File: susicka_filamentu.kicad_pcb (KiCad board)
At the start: 4 copper layers, 70 x 100 mm, 108 parts, among them J10 NTC 100k B3950, J11 SHT40 #2, J12 GPIO rezerva, J13 Tepelna pojistka, J2 Conn_01x03, J3 Conn_01x04, J4 PJ-102AH, J5 Topeni 24V, J6 SHT4x, J7 HX711, J8 Ventilator 24V, J9 Odtah 24V, Q1 SiS434DN, Q2 AO3422, Q3 AOD4185, Q4 AO3422, SW1 Tlacitko, U1 RP2350A-QFN60, U2 RM2, U3 W25Q128JVS, U4 AP63203WU, Y1 ABM8-272-T3 12MHz

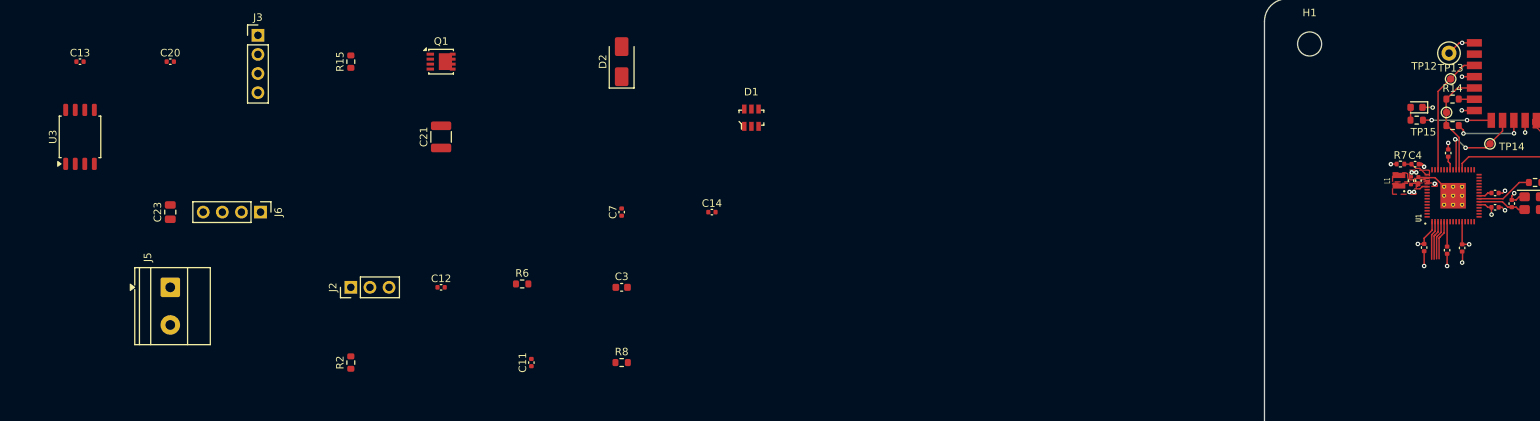
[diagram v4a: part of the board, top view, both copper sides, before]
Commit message: Place and route RP2350 decoupling capacitors
- C11 (pin 30), C13 (pins 44+45), C14 (pins 53+54) next to their pins
- C12 for pin 38 via +3V3 plane: pin 38 has a via under the package,
  C12 above C13 with its own +3V3 via and shared GND via
- C9/C16/C17/C8/C10/C15 kept; zones refilled (fixes GND via vs +1V1 zone clearance)

Co-Authored-By: Claude Opus 5.5 <noreply@anthropic.com>
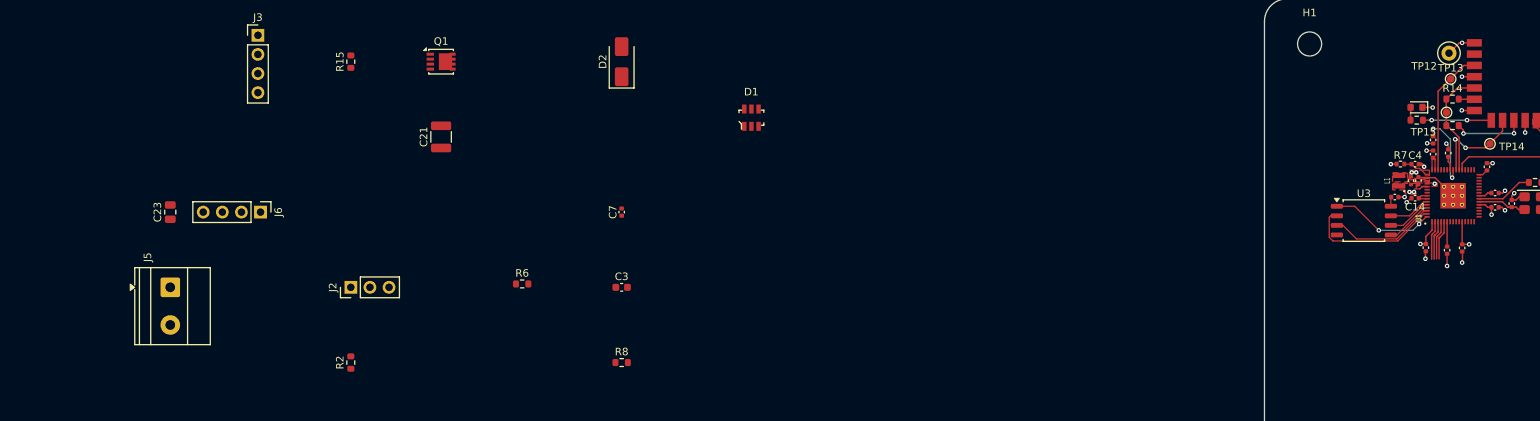
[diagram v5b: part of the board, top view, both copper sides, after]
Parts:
- moved C13 180.3 mm to (209.5, 58.5), turned to 90 degrees
- moved U3 171.0 mm to (200.3, 67.4), turned to 0 degrees
- moved C20 163.8 mm to (204.4, 64.2)
- moved C12 133.3 mm to (209.5, 56.6), turned to -90 degrees
- moved C11 129.7 mm to (216.7, 60.2)
- moved C14 93.5 mm to (207.1, 64.4), turned to 180 degrees
- moved C10 0.23 mm to (208.6, 71.0)
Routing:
- net /flash/QSPI_SD1: track 0.00 -> 19.4 mm
- net +3V3: track 18.1 -> 36.4 mm, vias 7 -> 9
- net /flash/QSPI_SD2: track 0.00 -> 14.4 mm
- net /flash/QSPI_SS: track 0.00 -> 14.1 mm, vias 0 -> 2
- net /flash/QSPI_SD0: track 0.00 -> 6.43 mm
- net /flash/QSPI_SCLK: track 0.00 -> 5.96 mm
- net /flash/QSPI_SD3: track 0.00 -> 5.60 mm
- net GND: track 37.1 -> 41.8 mm, vias 20 -> 25

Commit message: Update PCB layout (current working version)
Co-Authored-By: Claude Haiku 5.5 <noreply@anthropic.com>
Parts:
- moved C25 224.7 mm to (238.2, 91.0)
- moved D4 222.2 mm to (236.7, 104.9)
- moved R19 219.3 mm to (242.2, 105.2)
- moved F1 208.5 mm to (237.0, 121.5), turned to 90 degrees
- moved Q3 204.1 mm to (237.1, 112.6), turned to -90 degrees
- moved D5 198.1 mm to (237.2, 99.5), turned to 180 degrees
- moved L2 134.6 mm to (166.3, 99.9), turned to 90 degrees
- moved C22 126.9 mm to (163.0, 100.7), turned to 90 degrees
- moved C23 121.3 mm to (160.4, 90.8)
- moved U4 114.3 mm to (159.7, 101.1)
- moved C21 91.1 mm to (155.8, 103.1), turned to -90 degrees
- moved C24 82.3 mm to (164.8, 90.7)
- moved J4 27.6 mm to (241.2, 131.5)
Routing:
- net +1V1: track 8.51 -> 36.5 mm, vias 2 -> 5
- net +3V3: track 36.4 -> 48.9 mm, vias 9 -> 13
- net Net-(U4-SW): track 0.00 -> 5.77 mm
- net GND: track 41.8 -> 45.8 mm, vias 25 -> 35
- net Net-(U4-BST): track 0.00 -> 2.24 mm
- added copper zone on In2.Cu, net +3V3
- added copper zone on F.Cu, net 24V
- added copper zone on F.Cu, net 24V_IN
- added copper zone on In1.Cu, net GND
- added copper zone on In2.Cu, net GND
- added copper zone on F.Cu, net Net-(D4-A)
- added copper zone on F.Cu, net Net-(Q3-D)

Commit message: Layout: I2C pull-ups, test point properties, power section progress
- R21/R22 (I2C1) and R26/R27 (I2C0) placed and routed
- test point fabrication property on placed TPs
- J6 SDA/SCL order swapped in schematic for routing
- J1 (USB, DNP) excluded from board

Co-Authored-By: Claude Opus 5.5 <noreply@anthropic.com>
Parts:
- removed C3: 4,7n, Capacitor_SMD:C_0603_1608Metric
- removed D1: USBLC6-2SC6, digikey-footprints:SOT23-6L
- removed R2, R3: 5,1k, Resistor_SMD:R_0603_1608Metric
- removed R4, R5: 27, Resistor_SMD:R_0603_1608Metric
- removed R6: 1M, Resistor_SMD:R_0603_1608Metric
- moved J11 231.3 mm to (233.1, 80.5), turned to 180 degrees
- moved SW1 220.1 mm to (243.6, 69.8)
- moved C27 217.3 mm to (235.6, 79.3), turned to 90 degrees
- moved R27 210.1 mm to (225.4, 71.1), turned to -90 degrees
- moved R26 206.1 mm to (223.5, 73.5), turned to 90 degrees
- moved R22 194.5 mm to (210.4, 81.2), turned to 90 degrees
- moved R21 191.1 mm to (207.9, 81.2), turned to 90 degrees
- moved TP9 191.0 mm to (229.9, 72.0)
- moved TP8 188.4 mm to (229.7, 74.5)
- moved TP1 183.3 mm to (232.4, 91.7)
- moved TP10 179.6 mm to (217.0, 74.7)
- moved J3 179.1 mm to (231.5, 60.4)
- moved TP11 174.0 mm to (219.7, 74.5)
- moved TP2 170.0 mm to (213.8, 86.6)
- moved TP7 169.9 mm to (210.6, 74.2), turned to 90 degrees
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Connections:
- J6 pad 3: SDA -> SCL
- J6 pad 4: SCL -> SDA
- J7 pad 3: HX711_DT -> HX711_SCK
- J7 pad 4: HX711_SCK -> HX711_DT
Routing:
- net BTN: track 0.00 -> 31.6 mm, vias 0 -> 2
- net +3V3: track 48.9 -> 79.8 mm, vias 13 -> 28
- net SDA0: track 0.00 -> 22.9 mm
- net SCL0: track 0.00 -> 21.4 mm
- net Net-(J3-Pin_4): track 0.00 -> 20.9 mm, vias 0 -> 2
- net SWCLK: track 0.00 -> 17.5 mm
- net SWDIO: track 0.00 -> 17.1 mm
- net HX711_SCK: track 0.00 -> 16.0 mm
- net HX711_DT: track 0.00 -> 13.9 mm
- net GND: track 45.8 -> 59.6 mm, vias 35 -> 78
- net SDA: track 5.20 -> 13.9 mm
- net SCL: track 5.23 -> 13.4 mm
- net Net-(J2-Pin_2): track 0.00 -> 3.20 mm
- net Net-(U1-GPIO1): track 5.22 -> 8.15 mm
- net Net-(J2-Pin_1): track 0.00 -> 2.82 mm
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- removed copper zone on In2.Cu, net GND

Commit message: Layout review fixes and JLCPCB fabrication outputs
- In2: GND pour over the whole board (priority 0) below the 3V3 zones
- Silkscreen: +/- marks of J5, J8, J9 moved out from under the terminal
  blocks; D4 and TP13 labels moved to visible spots
- TP12 moved away from the RM2 antenna keep-out, J4 shifted up,
  R20 220R so the D6 LED is visible at 3.3 V
- NTC (J10, R25, C26, TP19) excluded from this prototype board
- gerber/: fresh Gerber + Excellon export, JLCPCB zip, ordering notes
- CLAUDE.md, .claude/pamet.md: review results and decisions

Co-Authored-By: Claude Opus 5.5 <noreply@anthropic.com>
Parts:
- removed C26: 100nF, Capacitor_SMD:C_0402_1005Metric
- removed J10: NTC 100k B3950, Connector_PinHeader_2.54mm:PinHeader_1x02_P2.54mm_Vertical
- removed R25: 22k, Resistor_SMD:R_0603_1608Metric
- removed TP19: NTC_ADC, TestPoint:TestPoint_Pad_D1.0mm
- removed TP3: +1V1, TestPoint:TestPoint_Pad_D1.5mm
- R20: value 1k -> 220
- moved J5 192.2 mm to (212.3, 132.0), turned to 0 degrees
- moved J13 178.7 mm to (224.0, 132.0)
- moved D3 174.7 mm to (201.1, 108.8), turned to 90 degrees
- moved R16 174.4 mm to (210.0, 114.9), turned to -90 degrees
- moved J12 174.1 mm to (243.9, 49.5)
- moved D7 174.1 mm to (200.9, 120.8), turned to 90 degrees
- moved R17 171.8 mm to (206.4, 104.5), turned to -90 degrees
- moved J8 170.6 mm to (193.8, 106.0), turned to -90 degrees
- moved R18 170.5 mm to (204.8, 104.5), turned to 90 degrees
- moved R15 170.4 mm to (212.4, 115.5), turned to 0 degrees
- moved TP4 167.3 mm to (249.5, 121.9)
- moved R23 167.3 mm to (206.6, 116.4), turned to -90 degrees
- moved R24 161.1 mm to (204.8, 116.4), turned to 90 degrees
- moved Q1 159.6 mm to (212.6, 119.7), turned to -90 degrees
- moved J9 159.0 mm to (193.8, 117.6), turned to -90 degrees
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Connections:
- J13 pad 1: 24V -> /vystupy/HEAT_V
- J13 pad 2: /vystupy/HEAT_V -> 24V
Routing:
- net 24V: track 0.00 -> 67.5 mm
- net HEAT_PWM: track 0.00 -> 61.3 mm, vias 0 -> 2
- net EXH_PWM: track 0.00 -> 54.0 mm, vias 0 -> 2
- net FAN_PWM: track 0.00 -> 43.5 mm, vias 0 -> 2
- net GP28: track 0.00 -> 36.4 mm, vias 0 -> 2
- net GP17: track 1.19 -> 36.9 mm
- net GP21: track 0.00 -> 34.1 mm, vias 0 -> 2
- net GP22: track 0.00 -> 32.7 mm
- net GND: track 59.6 -> 75.0 mm, vias 78 -> 224
- net BTN: track 31.6 -> 38.8 mm
- net +3V3: track 79.8 -> 82.0 mm, vias 28 -> 29
- net GP16: track 1.04 -> 0.00 mm, vias 1 -> 0
- net GP18: track 0.95 -> 0.00 mm, vias 1 -> 0
- added copper zone on F.Cu, net /vystupy/HEAT_V
- added copper zone on B.Cu, net GND
- added copper zone on In2.Cu, net GND
- added copper zone on F.Cu, net Net-(D2-A)
- added copper zone on F.Cu, net Net-(D3-A)
- added copper zone on F.Cu, net Net-(D7-A)
- added copper zone on F.Cu, net Net-(Q1-G)
- added copper zone on F.Cu, net Net-(Q2-G)
- added copper zone on F.Cu, net Net-(Q4-G)
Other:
- board text added: "+"
- board text added: "-"
- board text added: "17"
- board text added: "21"
- board text added: "22"
- board text added: "24V DC"
- board text added: "28"
- board text added: "3V3"
- board text added: "CLK"
- board text added: "DIO"
- board text added: "DT"
- board text added: "GND"
- board text added: "ODTAH"
- board text added: "RUN"
- board text added: "RX"
- board text added: "SCK"
- board text added: "SCL"
- board text added: "SDA"
- board text added: "SUSICKA FILAMENTU v1.0 2026"
- board text added: "TCO"
- board text added: "TOPENI"
- board text added: "TX"
- board text added: "VENT"
